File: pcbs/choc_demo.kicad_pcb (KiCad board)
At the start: 2 copper layers, 230 x 95 mm, 140 parts

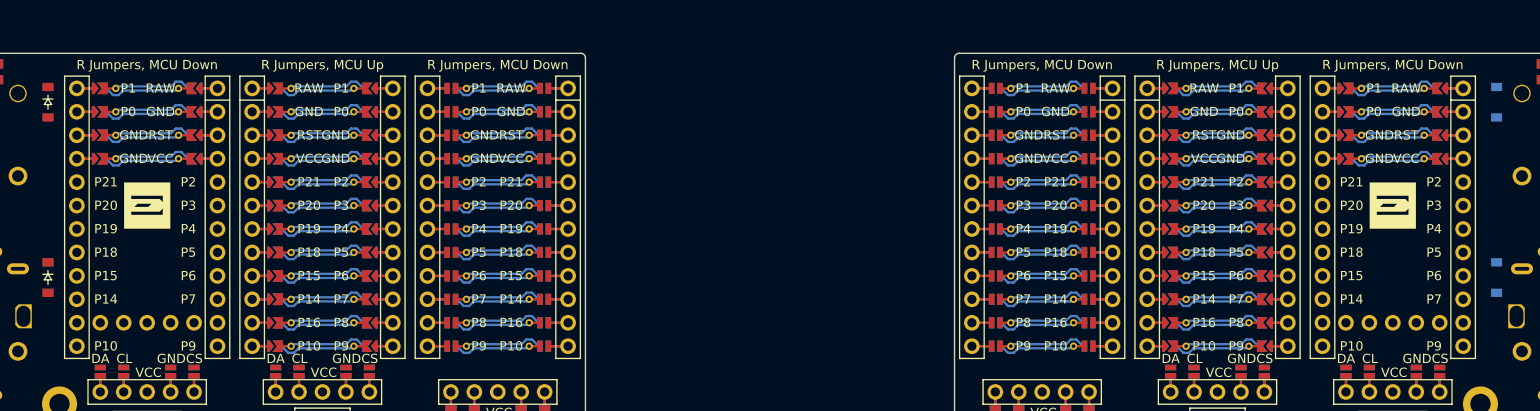
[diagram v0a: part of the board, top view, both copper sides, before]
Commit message: Rename demo board for Choc v1/v2 and add MX demo board
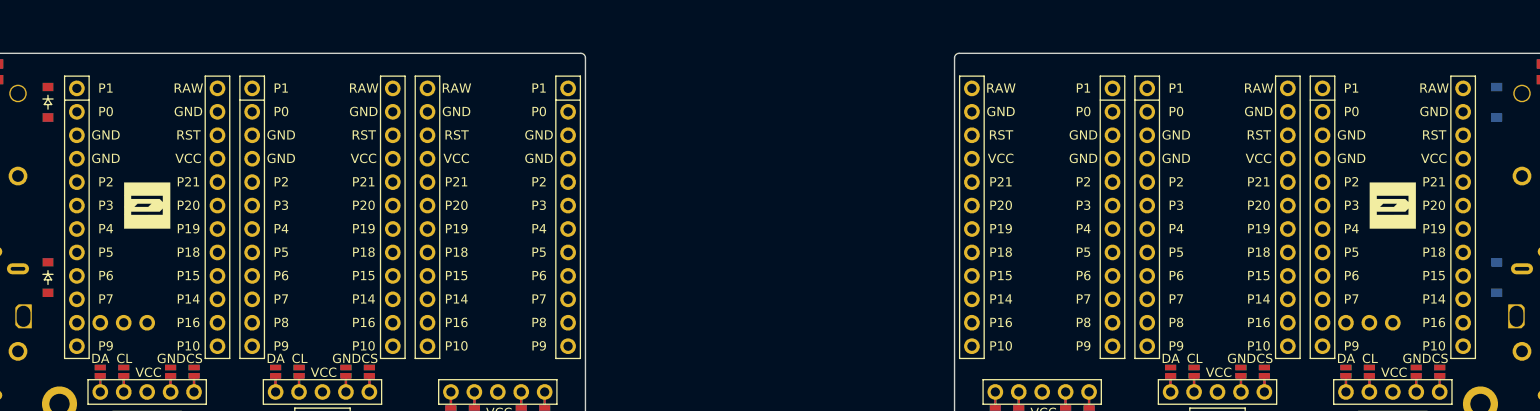
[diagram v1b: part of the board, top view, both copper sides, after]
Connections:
- MCU1 pad 1: MCU1_1 -> P1
- MCU1 pad 10: MCU1_10 -> P7
- MCU1 pad 11: MCU1_11 -> P8
- MCU1 pad 12: MCU1_12 -> P9
- MCU1 pad 13: MCU1_12 -> P10
- MCU1 pad 14: MCU1_11 -> P16
- MCU1 pad 15: MCU1_10 -> P14
- MCU1 pad 16: MCU1_9 -> P15
- MCU1 pad 17: MCU1_8 -> P18
- MCU1 pad 18: MCU1_7 -> P19
- MCU1 pad 19: MCU1_6 -> P20
- MCU1 pad 2: MCU1_2 -> P0
- MCU1 pad 20: MCU1_5 -> P21
- MCU1 pad 21: MCU1_4 -> VCC
- MCU1 pad 22: MCU1_3 -> RST
- MCU1 pad 23: MCU1_2 -> GND
- MCU1 pad 24: MCU1_1 -> RAW
- MCU1 pad 3: MCU1_3 -> GND
- MCU1 pad 4: MCU1_4 -> GND
- MCU1 pad 5: MCU1_5 -> P2
- MCU1 pad 6: MCU1_6 -> P3
- MCU1 pad 7: MCU1_7 -> P4
- MCU1 pad 8: MCU1_8 -> P5
- MCU1 pad 9: MCU1_9 -> P6
- MCU2 pad 1: MCU2_1 -> P1
- MCU2 pad 10: MCU2_10 -> P7
- MCU2 pad 11: MCU2_11 -> P8
- MCU2 pad 12: MCU2_12 -> P9
- MCU2 pad 13: MCU2_12 -> P10
- MCU2 pad 14: MCU2_11 -> P16
- MCU2 pad 15: MCU2_10 -> P14
- MCU2 pad 16: MCU2_9 -> P15
- MCU2 pad 17: MCU2_8 -> P18
- MCU2 pad 18: MCU2_7 -> P19
- MCU2 pad 19: MCU2_6 -> P20
- MCU2 pad 2: MCU2_2 -> P0
- MCU2 pad 20: MCU2_5 -> P21
- MCU2 pad 21: MCU2_4 -> VCC
- MCU2 pad 22: MCU2_3 -> RST
- MCU2 pad 23: MCU2_2 -> GND
- MCU2 pad 24: MCU2_1 -> RAW
- MCU2 pad 3: MCU2_3 -> GND
- MCU2 pad 4: MCU2_4 -> GND
- MCU2 pad 5: MCU2_5 -> P2
- MCU2 pad 6: MCU2_6 -> P3
- MCU2 pad 7: MCU2_7 -> P4
- MCU2 pad 8: MCU2_8 -> P5
- MCU2 pad 9: MCU2_9 -> P6
- MCU3 pad 1: MCU3_1 -> RAW
- MCU3 pad 10: MCU3_10 -> P14
- MCU3 pad 11: MCU3_11 -> P16
- MCU3 pad 12: MCU3_12 -> P10
- MCU3 pad 13: MCU3_13 -> P9
- MCU3 pad 14: MCU3_14 -> P8
- MCU3 pad 15: MCU3_15 -> P7
- MCU3 pad 16: MCU3_16 -> P6
- MCU3 pad 17: MCU3_17 -> P5
- MCU3 pad 18: MCU3_18 -> P4
- MCU3 pad 19: MCU3_19 -> P3
- MCU3 pad 2: MCU3_2 -> GND
- MCU3 pad 20: MCU3_20 -> P2
- MCU3 pad 21: MCU3_21 -> GND
- MCU3 pad 22: MCU3_22 -> GND
- MCU3 pad 23: MCU3_23 -> P0
- MCU3 pad 24: MCU3_24 -> P1
- MCU3 pad 3: MCU3_3 -> RST
- MCU3 pad 4: MCU3_4 -> VCC
- MCU3 pad 5: MCU3_5 -> P21
- MCU3 pad 6: MCU3_6 -> P20
- MCU3 pad 7: MCU3_7 -> P19
- MCU3 pad 8: MCU3_8 -> P18
- MCU3 pad 9: MCU3_9 -> P15
- MCU4 pad 1: MCU4_1 -> RAW
- MCU4 pad 10: MCU4_10 -> P14
- MCU4 pad 11: MCU4_11 -> P16
- MCU4 pad 12: MCU4_12 -> P10
- MCU4 pad 13: MCU4_13 -> P9
- MCU4 pad 14: MCU4_14 -> P8
- MCU4 pad 15: MCU4_15 -> P7
- MCU4 pad 16: MCU4_16 -> P6
- MCU4 pad 17: MCU4_17 -> P5
- MCU4 pad 18: MCU4_18 -> P4
- MCU4 pad 19: MCU4_19 -> P3
- MCU4 pad 2: MCU4_2 -> GND
- MCU4 pad 20: MCU4_20 -> P2
- MCU4 pad 21: MCU4_21 -> GND
- MCU4 pad 22: MCU4_22 -> GND
- MCU4 pad 23: MCU4_23 -> P0
- MCU4 pad 24: MCU4_24 -> P1
- MCU4 pad 3: MCU4_3 -> RST
- MCU4 pad 4: MCU4_4 -> VCC
- MCU4 pad 5: MCU4_5 -> P21
- MCU4 pad 6: MCU4_6 -> P20
- MCU4 pad 7: MCU4_7 -> P19
- MCU4 pad 8: MCU4_8 -> P18
- MCU4 pad 9: MCU4_9 -> P15
- MCU5 pad 1: MCU5_1 -> RAW
- MCU5 pad 10: P7 -> P14
- MCU5 pad 11: P8 -> P16
- MCU5 pad 12: P9 -> P10
- MCU5 pad 13: P10 -> P9
- MCU5 pad 14: P16 -> P8
- MCU5 pad 15: P14 -> P7
- MCU5 pad 16: P15 -> P6
- MCU5 pad 17: P18 -> P5
- MCU5 pad 18: P19 -> P4
- MCU5 pad 19: P20 -> P3
- MCU5 pad 2: MCU5_2 -> GND
- MCU5 pad 20: P21 -> P2
- MCU5 pad 21: MCU5_21 -> GND
- MCU5 pad 22: MCU5_22 -> GND
- MCU5 pad 23: MCU5_23 -> P0
- MCU5 pad 24: MCU5_24 -> P1
- MCU5 pad 3: MCU5_3 -> RST
- MCU5 pad 4: MCU5_4 -> VCC
- MCU5 pad 5: P2 -> P21
- MCU5 pad 6: P3 -> P20
- MCU5 pad 7: P4 -> P19
- MCU5 pad 8: P5 -> P18
- MCU5 pad 9: P6 -> P15
- MCU6 pad 1: MCU6_1 -> RAW
- MCU6 pad 10: P7 -> P14
- MCU6 pad 11: P8 -> P16
- MCU6 pad 12: P9 -> P10
- MCU6 pad 13: P10 -> P9
- MCU6 pad 14: P16 -> P8
- MCU6 pad 15: P14 -> P7
- MCU6 pad 16: P15 -> P6
- MCU6 pad 17: P18 -> P5
- MCU6 pad 18: P19 -> P4
- MCU6 pad 19: P20 -> P3
- MCU6 pad 2: MCU6_2 -> GND
- MCU6 pad 20: P21 -> P2
- MCU6 pad 21: MCU6_21 -> GND
- MCU6 pad 22: MCU6_22 -> GND
- MCU6 pad 23: MCU6_23 -> P0
- MCU6 pad 24: MCU6_24 -> P1
- MCU6 pad 3: MCU6_3 -> RST
- MCU6 pad 4: MCU6_4 -> VCC
- MCU6 pad 5: P2 -> P21
- MCU6 pad 6: P3 -> P20
- MCU6 pad 7: P4 -> P19
- MCU6 pad 8: P5 -> P18
- MCU6 pad 9: P6 -> P15
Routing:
- net (no net): track 1566.8 -> 0.00 mm
